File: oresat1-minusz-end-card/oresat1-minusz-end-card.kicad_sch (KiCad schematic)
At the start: 35 parts, among them J1 J-SAMTEC-TFM-120-01-L-D-RA, J2 U.FL-R-SMT-1, J3 Harwin M55-7101242R, J5 Harwin M55-7101242R

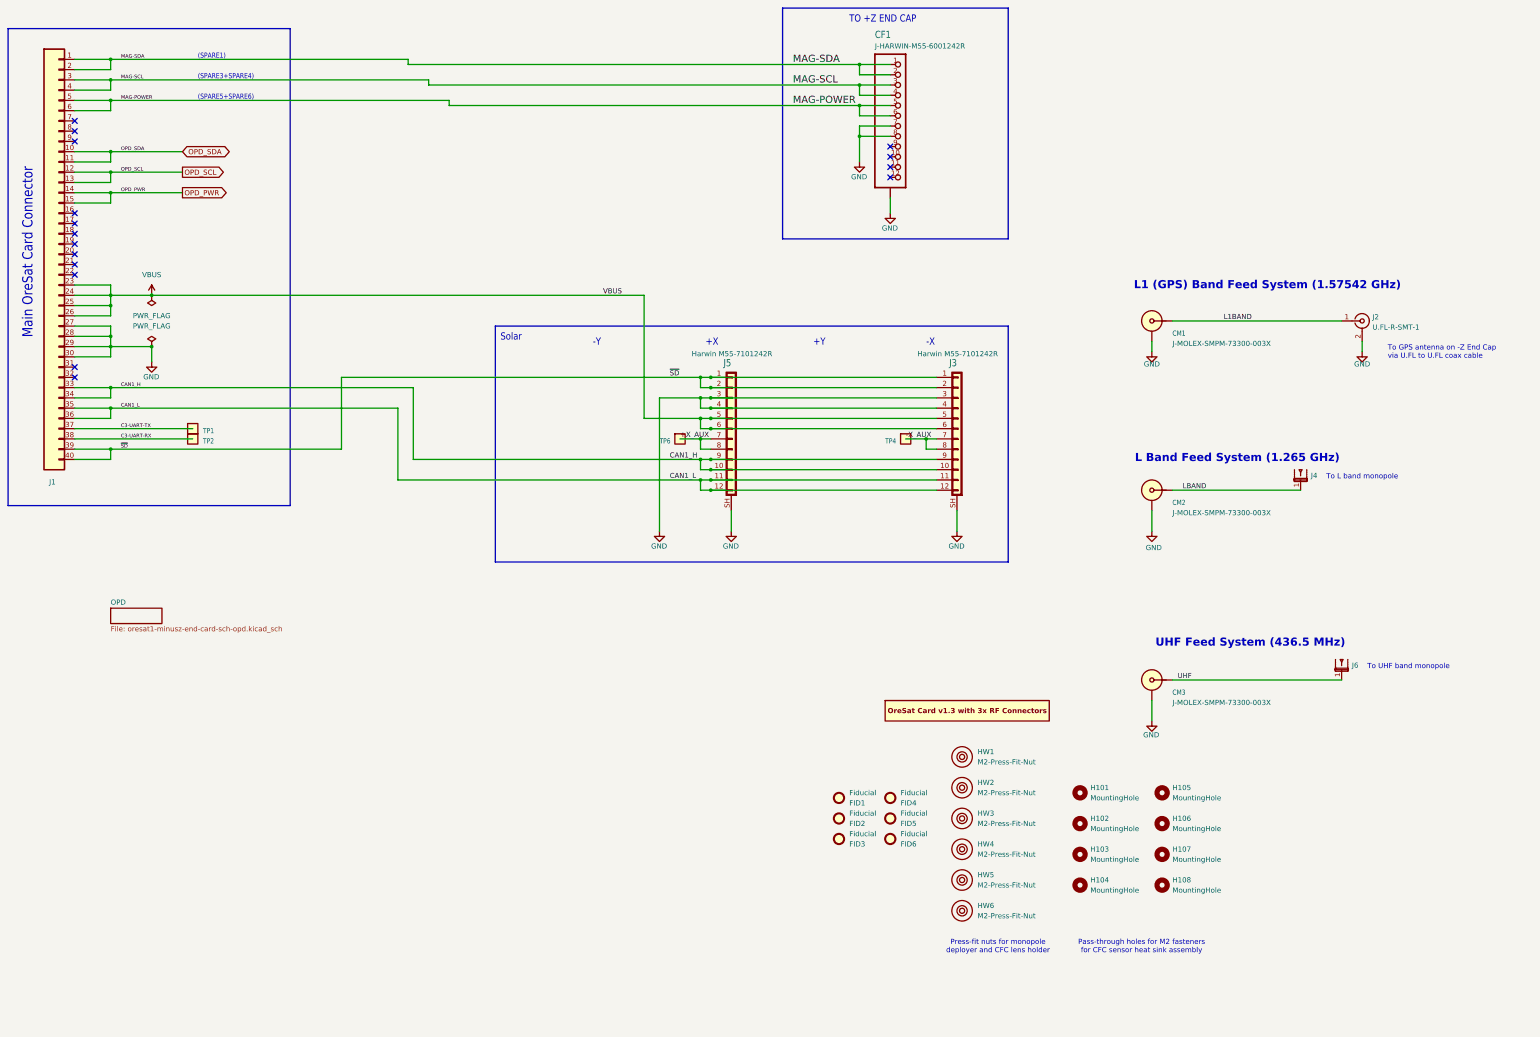
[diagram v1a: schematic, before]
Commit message: OreSat1 -Z end card update
Upgraded symbols, fixed BOM and added presets, and added UART switches for new solar modules. Clleaned up layout, including some planes and footprints. Still more left to do, but it's more ready to go.
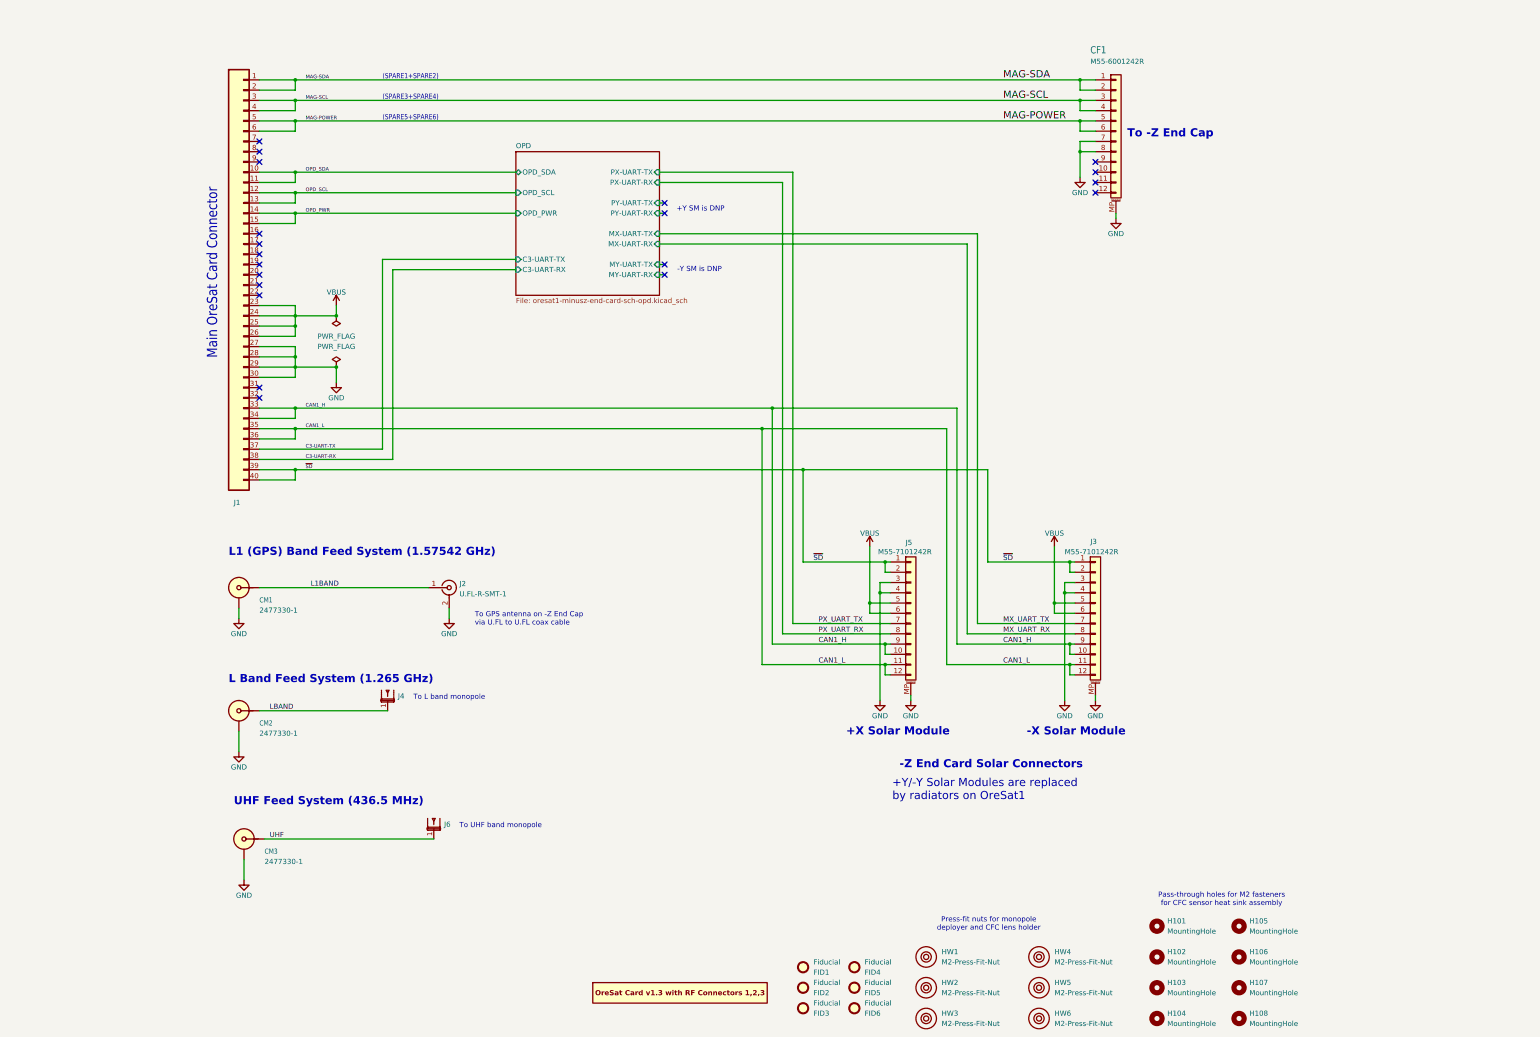
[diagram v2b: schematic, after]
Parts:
- removed TP1, TP2, TP4, TP6: TEST-POINT-LARGE-SQUARE, oresat-misc:TestPoint-0.75mm-th, symbol oresat-misc:Test-Point-0.75mm-th
- CF1: value J-HARWIN-M55-6001242R -> M55-6001242R; symbol oresat-connectors:J-HARWIN-M55-6001242R -> Connector_Generic_MountingPin:Conn_01x12_MountingPin; DIS (none) -> DigiKey; DPN (none) -> 952-3835-1-ND; MFR (none) -> Harwin; MPN (none) -> M55-6001242R
- CM1, CM2, CM3: value J-MOLEX-SMPM-73300-003X -> 2477330-1; DIS (none) -> DigiKey; DPN (none) -> 343-2477330-1CT-ND; MFR (none) -> TE Connectivity Linx; MPN (none) -> 2477330-1
- FID1, FID2, FID3, FID4, FID5, FID6, J4, J6, PCB1: now left out of the parts list
- HW1, HW2, HW3, HW4, HW5, HW6: DIS (none) -> McMaster-Carr; DPN (none) -> 94100A150; MFR (none) -> N/A; MPN (none) -> N/A
- J1: DIS (none) -> DigiKey; DPN (none) -> SAM10145-ND; MFR (none) -> Samtec; MPN (none) -> TFM-120-01-L-D-RA
- J2: DIS (none) -> DigiKey; DPN (none) -> H11891CT-ND; MFR (none) -> Hirose; MPN (none) -> U.FL-R-SMT-1(10)
- J3, J5: value Harwin M55-7101242R -> M55-7101242R; symbol oresat-connectors:Harwin M55-7101242R -> Connector_Generic_MountingPin:Conn_01x12_MountingPin; DIS (none) -> DigiKey; DPN (none) -> 952-3891-1-ND; MFR (none) -> Harwin; MPN (none) -> M55-7101242R
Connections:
- net GND: now also CF1.MP (MountPin), J3.MP (MountPin), J5.MP (MountPin); no longer CF1.SH (SHIELD), J3.SH (Shield), J5.SH (Shield)
- net +X_AUX renamed PX_UART_RX
- net PX_UART_RX: no longer J5.7 (Pin_7)
- net -X_AUX renamed MX_UART_RX
- net MX_UART_RX: no longer J3.7 (Pin_7)
- new net MX_UART_TX: J3.7 (Pin_7)
- new net PX_UART_TX: J5.7 (Pin_7)
- no-connect marks 16 -> 20
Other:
- sheet OPD ports: added C3-UART-RX, C3-UART-TX, MX-UART-RX, MX-UART-TX, MY-UART-RX, MY-UART-TX, OPD_PWR, OPD_SCL, OPD_SDA, PX-UART-RX, PX-UART-TX, PY-UART-RX, PY-UART-TX; removed none
- note added: "(SPARE1+SPARE2)"
- note added: "+X Solar Module"
- note added: "+Y SM is DNP"
- note added: "+Y/-Y Solar Modules are replaced by radiators on OreSat1"
- note added: "-X Solar Module"
- note added: "-Y SM is DNP"
- note added: "-Z End Card Solar Connectors"
- note added: "To -Z End Cap"
- note removed: "(SPARE1)"
- note removed: "+X"
- note removed: "+Y"
- note removed: "-X"
- note removed: "-Y"
- note removed: "Solar"
- note removed: "TO +Z END CAP"
- moved on the sheet: CM1, CM2, CM3, FID1, FID2, FID3, FID4, FID5, FID6, H101, H102, H103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

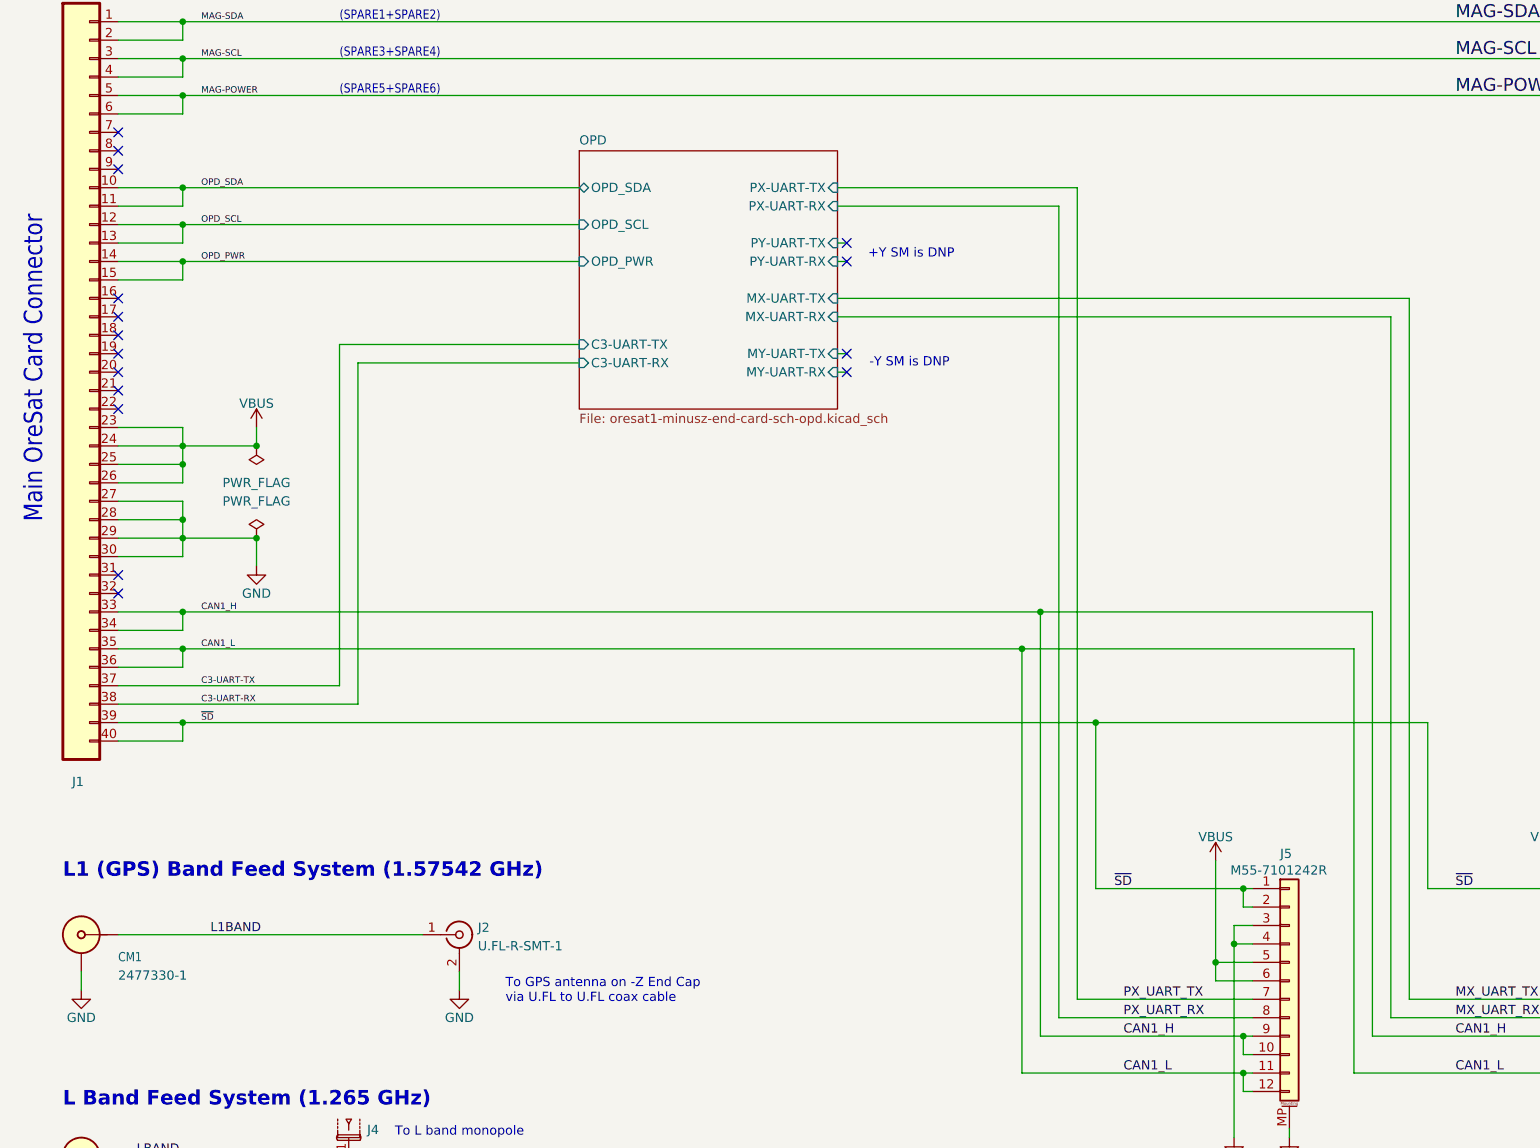
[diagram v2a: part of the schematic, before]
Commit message: FIxed OPD connection
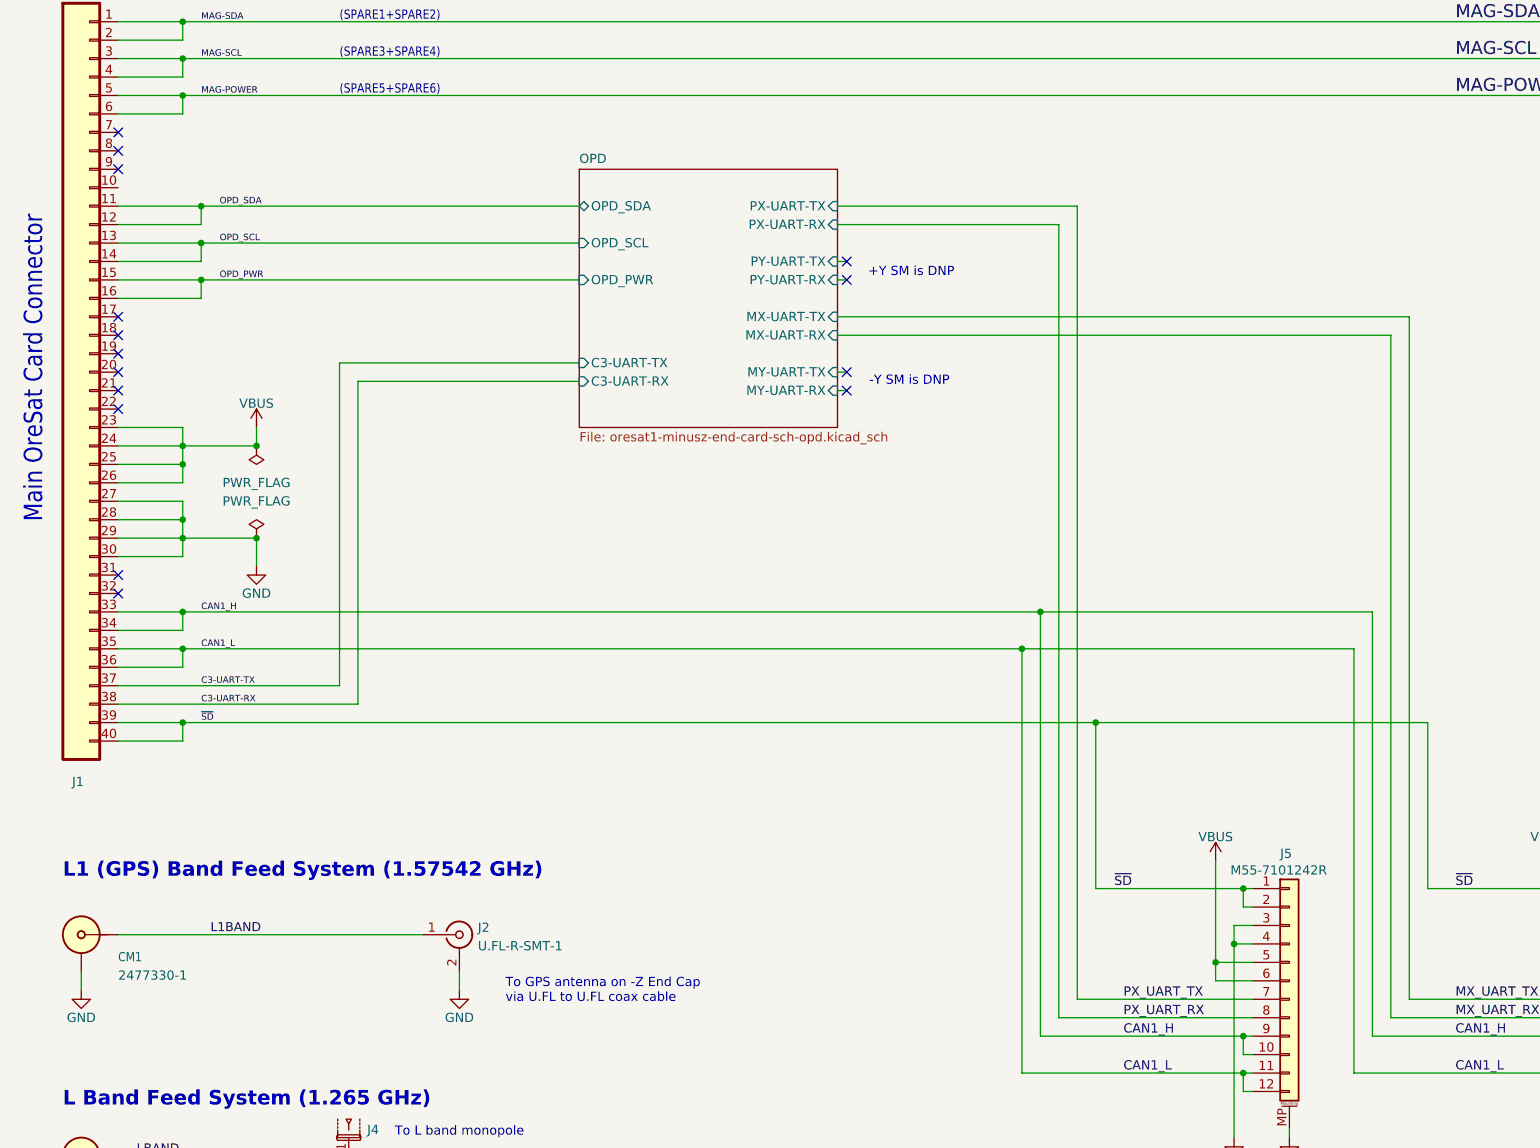
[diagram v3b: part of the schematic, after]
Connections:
- net OPD_PWR: now also J1.16; no longer J1.14
- net OPD_SCL: now also J1.14; no longer J1.12
- net OPD_SDA: now also J1.12; no longer J1.10
- no-connect marks 20 -> 19
